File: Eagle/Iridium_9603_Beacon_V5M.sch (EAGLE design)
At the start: 99 parts, among them CON4 uFL, J1 SS4-10-3.50-X-D, Q1 DMG3415U-7, Q2 DMG3415U-7, Q3 DMG3415U-7, Q4 DMG3415U-7, Q5 2N2222, U1 MCP111T-240E/TT, U2 SPX3819-3.3, U3 LTC3225EDDB#TRMPBF, U4 MPL3115A2LGA8, U5 ATSAMD21G18_QFN, U6 MAX-M8, U7 LT1634-1,25BMCMS8, X1 32.768

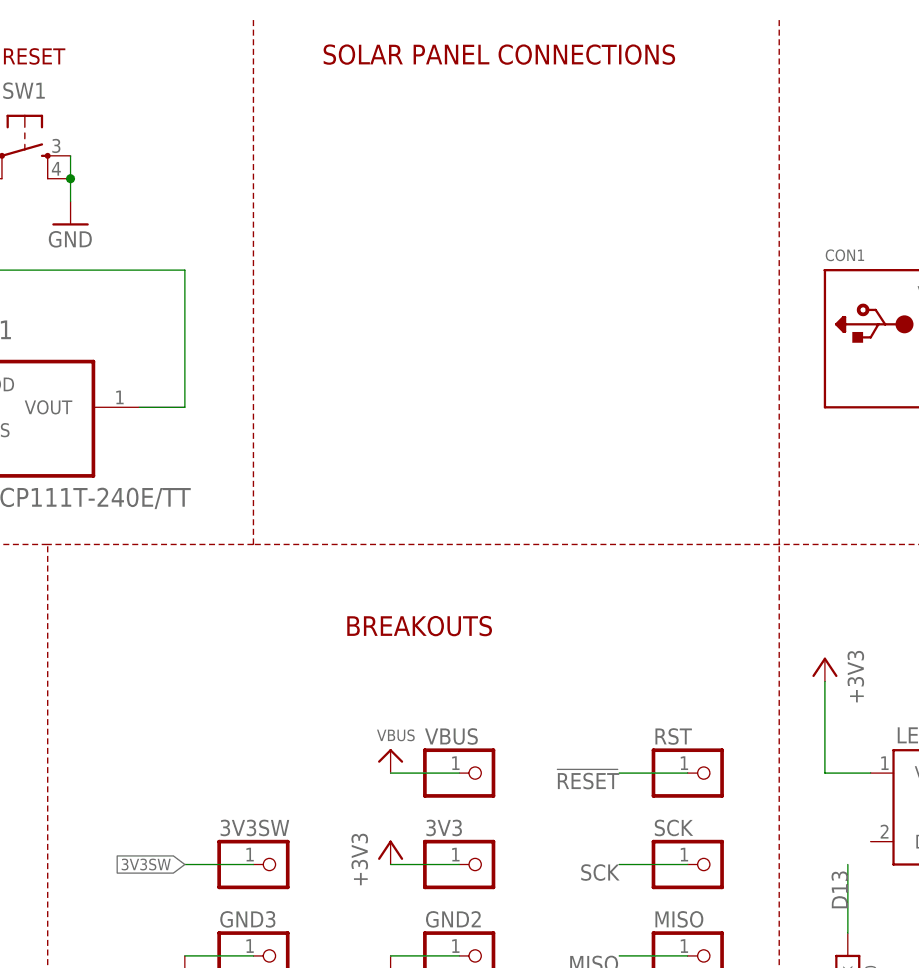
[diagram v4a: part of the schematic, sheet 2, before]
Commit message: several changes to the board layout. Switched digital I/O lines for coil reset and charger shutdown.  Added extra serial port.
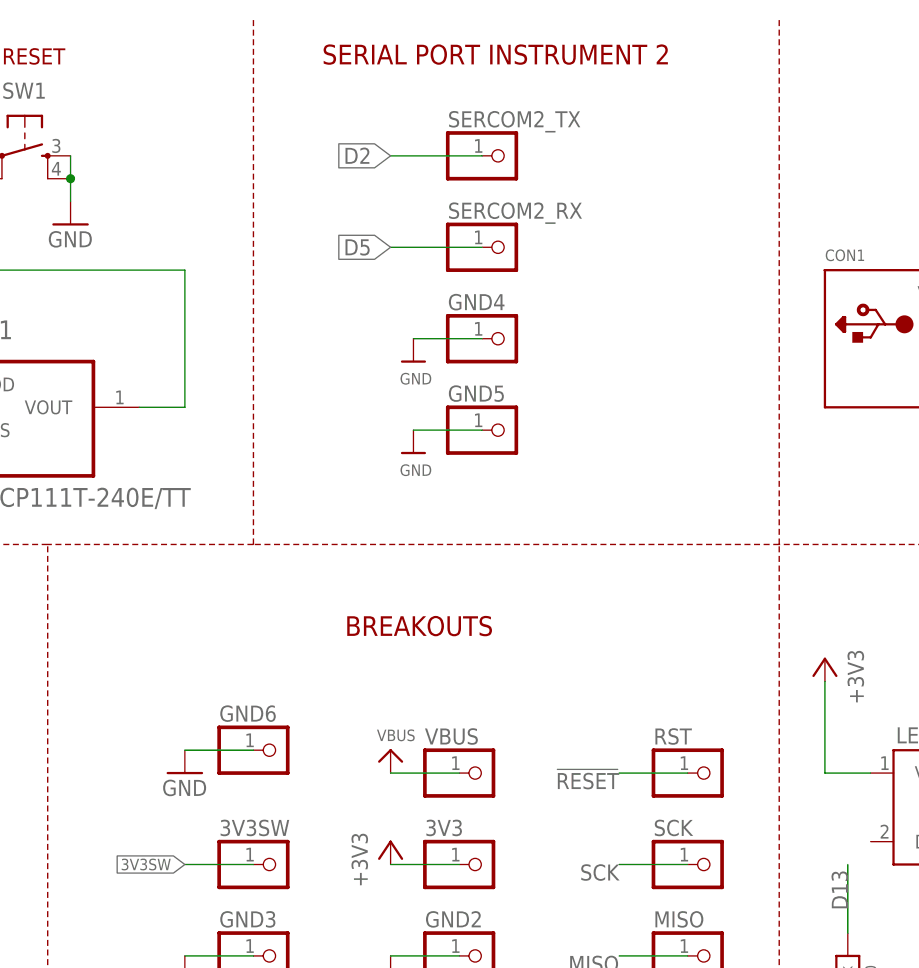
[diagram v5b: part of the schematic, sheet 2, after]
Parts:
- added GND4, GND5, GND6, SERCOM2_RX, SERCOM2_TX: (no value), adafruit:PINHD-1X1
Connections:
- net D2: now also SERCOM2_TX.1; no longer Q3.G, R13.1
- net D3: now also Q3.G, R13.1
- net D5: now also SERCOM2_RX.1; no longer R16.1, U3.~SHDN
- net D8: now also R16.1, U3.~SHDN
- net GND: now also GND4.1, GND5.1, GND6.1
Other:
- note added: "SERIAL PORT INSTRUMENT 2"
- note added: "V5M: Double AA battery capacity Added mounting holes (M3) Added SPDT Switch for power Removed Solar Power connections Moved Reset Switch to Bottom Moved D2 to D3 [Coil RESET] Moved D5 to D8 [LTC3225shutdown] Added Serial TX and RX, SERCOM2 on Pins 23 and 24"
- note removed: "SOLAR PANEL CONNECTIONS"
- note removed: "V5M: Double AA battery capacity Added mounting holes (M3) Added SPDT Switch for power Removed Solar Power connections Moved Reset Switch to Bottom"
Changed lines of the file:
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@@
 <part name="U$53" library="argol-eagle-library" deviceset="7101K2AV2QE" device=""/>
 <part name="FD3" library="SparkFun-Aesthetics" deviceset="FIDUCIAL" device="1X2"/>
+<part name="SERCOM2_TX" library="adafruit" library_urn="urn:adsk.eagle:library:420" deviceset="PINHD-1X1" device="" package3d_urn="urn:adsk.eagle:package:6240654/1"/>
+<part name="GND4" library="adafruit" library_urn="urn:adsk.eagle:library:420" deviceset="PINHD-1X1" device="" package3d_urn="urn:adsk.eagle:package:6240654/1"/>
+<part name="GND5" library="adafruit" library_urn="urn:adsk.eagle:library:420" deviceset="PINHD-1X1" device="" package3d_urn="urn:adsk.eagle:package:6240654/1"/>
+<part name="SERCOM2_RX" library="adafruit" library_urn="urn:adsk.eagle:library:420" deviceset="PINHD-1X1" device="" package3d_urn="urn:adsk.eagle:package:6240654/1"/>
+<part name="U$34" library="microbuilder" deviceset="GND" device=""/>
+<part name="U$54" library="microbuilder" deviceset="GND" device=""/>
+<part name="GND6" library="adafruit" library_urn="urn:adsk.eagle:library:420" deviceset="PINHD-1X1" device="" package3d_urn="urn:adsk.eagle:package:6240654/1"/>
+<part name="GND14" library="supply1" library_urn="urn:adsk.eagle:library:371" deviceset="GND" device=""/>
 </parts>
 <sheets>
@@
 <wire x1="134.62" y1="38.1" x2="134.62" y2="116.84" width="0.1524" layer="94" style="shortdash"/>
 <text x="238.76" y="76.2" size="2.1844" layer="94" align="bottom-center">WS2812B</text>
-<text x="165.1" y="170.18" size="2.1844" layer="94">SOLAR PANEL CONNECTIONS</text>
+<text x="165.1" y="170.18" size="2.1844" layer="94">SERIAL PORT INSTRUMENT 2</text>
 </plain>
 <instances>
@@
 <attribute name="VALUE" x="201.93" y="86.36" size="1.778" layer="96"/>
 </instance>
+<instance part="SERCOM2_TX" gate="G$1" x="185.42" y="160.02" smashed="yes">
+<attribute name="NAME" x="179.07" y="163.195" size="1.778" layer="95"/>
+<attribute name="VALUE" x="179.07" y="154.94" size="1.778" layer="96"/>
+</instance>
+<instance part="GND4" gate="G$1" x="185.42" y="139.7" smashed="yes">
+<attribute name="NAME" x="179.07" y="142.875" size="1.778" layer="95"/>
+<attribute name="VALUE" x="179.07" y="134.62" size="1.778" layer="96"/>
+</instance>
+<instance part="GND5" gate="G$1" x="185.42" y="129.54" smashed="yes">
+<attribute name="NAME" x="179.07" y="132.715" size="1.778" layer="95"/>
+<attribute name="VALUE" x="179.07" y="124.46" size="1.778" layer="96"/>
+</instance>
+<instance part="SERCOM2_RX" gate="G$1" x="185.42" y="149.86" smashed="yes">
+<attribute name="NAME" x="179.07" y="153.035" size="1.778" layer="95"/>
+<attribute name="VALUE" x="179.07" y="144.78" size="1.778" layer="96"/>
+</instance>
+<instance part="U$34" gate="G$1" x="175.26" y="127" smashed="yes">
+<attribute name="VALUE" x="173.736" y="124.46" size="1.27" layer="96"/>
+</instance>
+<instance part="U$54" gate="G$1" x="175.26" y="137.16" smashed="yes">
+<attribute name="VALUE" x="173.736" y="134.62" size="1.27" layer="96"/>
+</instance>
+<instance part="GND6" gate="G$1" x="160.02" y="93.98" smashed="yes">
+<attribute name="NAME" x="153.67" y="97.155" size="1.778" layer="95"/>
+<attribute name="VALUE" x="153.67" y="88.9" size="1.778" layer="96"/>
+</instance>
+<instance part="GND14" gate="1" x="149.86" y="91.44" smashed="yes">
+<attribute name="VALUE" x="147.32" y="88.9" size="1.778" layer="96"/>
+</instance>
 </instances>
 <busses>
@@
 <pinref part="GND9" gate="1" pin="GND"/>
 <wire x1="223.52" y1="53.34" x2="223.52" y2="48.26" width="0.1524" layer="91"/>
+</segment>
+<segment>
+<pinref part="U$54" gate="G$1" pin="GND"/>
+<pinref part="GND4" gate="G$1" pin="1"/>
+<wire x1="175.26" y1="139.7" x2="182.88" y2="139.7" width="0.1524" layer="91"/>
+</segment>
+<segment>
+<pinref part="U$34" gate="G$1" pin="GND"/>
+<pinref part="GND5" gate="G$1" pin="1"/>
+<wire x1="175.26" y1="129.54" x2="182.88" y2="129.54" width="0.1524" layer="91"/>
+</segment>
+<segment>
+<pinref part="GND14" gate="1" pin="GND"/>
+<pinref part="GND6" gate="G$1" pin="1"/>
+<wire x1="149.86" y1="93.98" x2="157.48" y2="93.98" width="0.1524" layer="91"/>
 </segment>
 </net>
@@
 <label x="109.22" y="50.8" size="1.778" layer="95"/>
 </segment>
+<segment>
+<pinref part="SERCOM2_RX" gate="G$1" pin="1"/>
+<wire x1="182.88" y1="149.86" x2="172.72" y2="149.86" width="0.1524" layer="91"/>
+<label x="172.72" y="149.86" size="1.778" layer="95" rot="R180" xref="yes"/>
+</segment>
 </net>
 <net name="D1" class="0">
@@
 <wire x1="101.6" y1="53.34" x2="119.38" y2="53.34" width="0.1524" layer="91"/>
 <label x="109.22" y="53.34" size="1.778" layer="95"/>
+</segment>
+<segment>
+<pinref part="SERCOM2_TX" gate="G$1" pin="1"/>
+<wire x1="182.88" y1="160.02" x2="172.72" y2="160.02" width="0.1524" layer="91"/>
+<label x="172.72" y="160.02" size="1.778" layer="95" rot="R180" xref="yes"/>
 </segment>
 </net>
@@
 </busses>
 <nets>
-<net name="D5" class="0">
-<segment>
-<label x="68.58" y="111.76" size="1.27" layer="95" rot="R180" xref="yes"/>
-<pinref part="U3" gate="G$1" pin="~SHDN"/>
-<wire x1="68.58" y1="111.76" x2="71.12" y2="111.76" width="0.1524" layer="91"/>
-<pinref part="R16" gate="G$1" pin="1"/>
-<wire x1="71.12" y1="111.76" x2="83.82" y2="111.76" width="0.1524" layer="91"/>
-<wire x1="71.12" y1="101.6" x2="71.12" y2="111.76" width="0.1524" layer="91"/>
-<junction x="71.12" y="111.76"/>
-</segment>
-</net>
 <net name="N$9" class="0">
 <segment>
@@
 </segment>
 </net>
+<net name="D8" class="0">
+<segment>
+<label x="68.58" y="111.76" size="1.27" layer="95" rot="R180" xref="yes"/>
+<pinref part="U3" gate="G$1" pin="~SHDN"/>
+<wire x1="68.58" y1="111.76" x2="71.12" y2="111.76" width="0.1524" layer="91"/>
+<pinref part="R16" gate="G$1" pin="1"/>
+<wire x1="71.12" y1="111.76" x2="83.82" y2="111.76" width="0.1524" layer="91"/>
+<wire x1="71.12" y1="101.6" x2="71.12" y2="111.76" width="0.1524" layer="91"/>
+<junction x="71.12" y="111.76"/>
+</segment>
+</net>
 </nets>
 </sheet>
@@
 </segment>
 </net>
-<net name="D2" class="0">
-<segment>
-<pinref part="Q3" gate="G$1" pin="G"/>
-<pinref part="R13" gate="G$1" pin="1"/>
-<wire x1="71.12" y1="101.6" x2="63.5" y2="101.6" width="0.1524" layer="91"/>
-<wire x1="63.5" y1="101.6" x2="48.26" y2="101.6" width="0.1524" layer="91"/>
-<junction x="63.5" y="101.6"/>
-<label x="48.26" y="101.6" size="1.778" layer="95" rot="R180" xref="yes"/>
-</segment>
-</net>
 <net name="RESET_RELAY" class="0">
 <segment>
@@
 <junction x="101.6" y="134.62"/>
 <label x="88.9" y="134.62" size="1.778" layer="95" rot="R180" xref="yes"/>
+</segment>
+</net>
+<net name="D3" class="0">
+<segment>
+<pinref part="Q3" gate="G$1" pin="G"/>
+<pinref part="R13" gate="G$1" pin="1"/>
+<wire x1="71.12" y1="101.6" x2="63.5" y2="101.6" width="0.1524" layer="91"/>
+<wire x1="63.5" y1="101.6" x2="50.8" y2="101.6" width="0.1524" layer="91"/>
+<junction x="63.5" y="101.6"/>
+<label x="50.8" y="101.6" size="1.778" layer="95" rot="R180" xref="yes"/>
 </segment>
 </net>
@@
 Added a pad for an external reset switch
 Added a pad for a battery power switch</text>
-<text x="157.48" y="149.86" size="2.54" layer="91" align="top-left">V5M:
+<text x="170.18" y="149.86" size="2.54" layer="91" align="top-left">V5M:
 Double AA battery capacity
 Added mounting holes (M3)
 Added SPDT Switch for power
 Removed Solar Power connections
-Moved Reset Switch to Bottom</text>
+Moved Reset Switch to Bottom
+Moved D2 to D3 [Coil RESET]
+Moved D5 to D8 [LTC3225shutdown]
+Added Serial TX and RX, SERCOM2 on Pins 23 and 24</text>
 </plain>
 <instances>

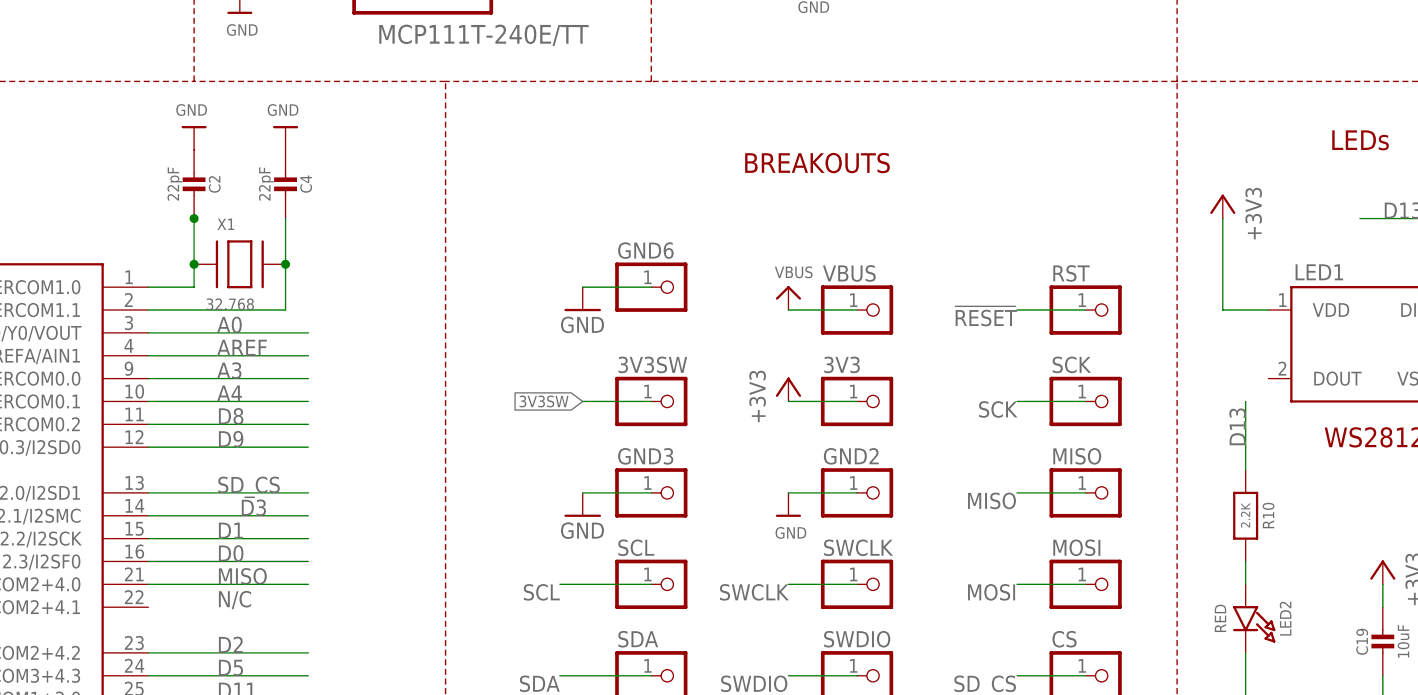
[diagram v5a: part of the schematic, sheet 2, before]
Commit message: updated CAD file, BOM, Gerber files generated for initial version of the board
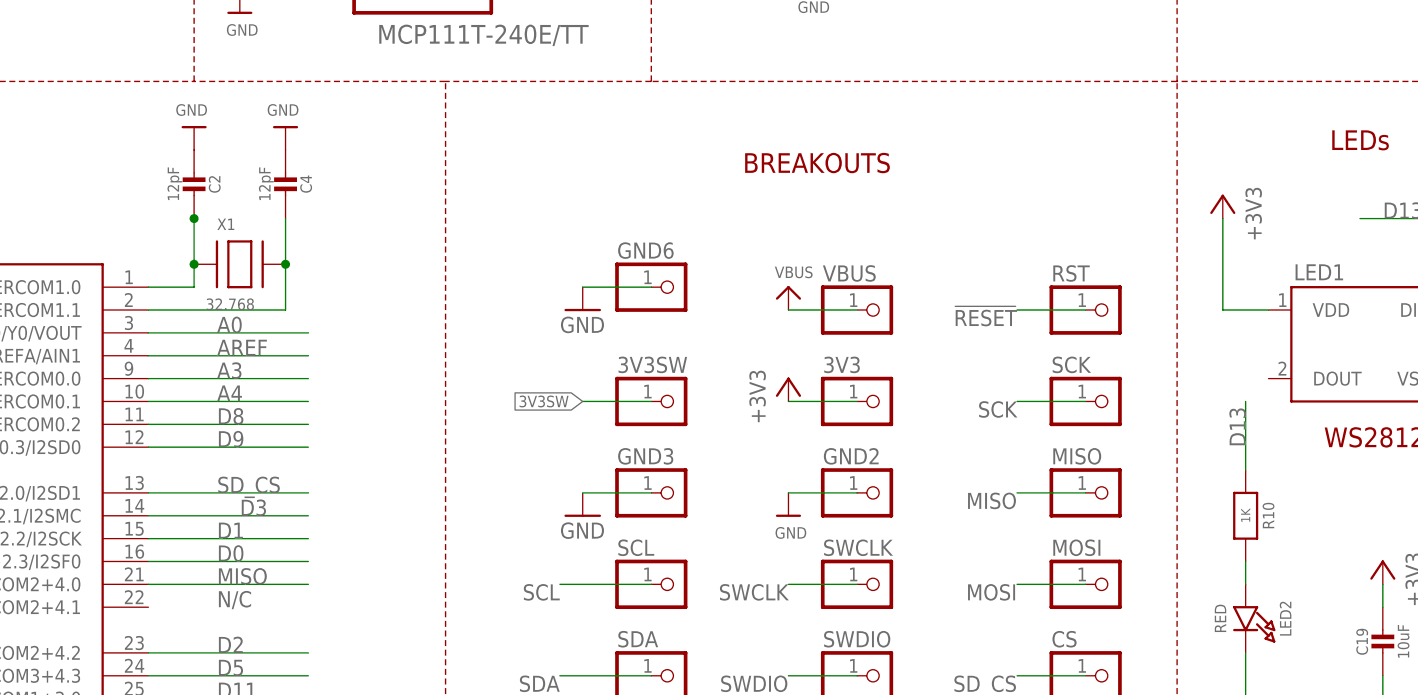
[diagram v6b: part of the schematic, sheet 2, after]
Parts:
- C2, C4: value 22pF -> 12pF
- R10: value 2.2K -> 1K
- renumbered U$53 to U53
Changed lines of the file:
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@@
 <part name="C1" library="microbuilder" deviceset="CAP_CERAMIC" device="0603_NO" value="1uF"/>
 <part name="U$6" library="microbuilder" deviceset="GND" device=""/>
-<part name="C2" library="microbuilder" deviceset="CAP_CERAMIC" device="0603_NO" value="22pF"/>
-<part name="C4" library="microbuilder" deviceset="CAP_CERAMIC" device="0603_NO" value="22pF"/>
+<part name="C2" library="microbuilder" deviceset="CAP_CERAMIC" device="0603_NO" value="12pF"/>
+<part name="C4" library="microbuilder" deviceset="CAP_CERAMIC" device="0603_NO" value="12pF"/>
 <part name="U$8" library="microbuilder" deviceset="GND" device=""/>
 <part name="U$10" library="microbuilder" deviceset="GND" device=""/>
@@
 <part name="U$44" library="microbuilder" deviceset="GND" device=""/>
 <part name="LED2" library="microbuilder" deviceset="LED" device="0805_NOOUTLINE" value="RED"/>
-<part name="R10" library="microbuilder" deviceset="RESISTOR" device="_0603_NOOUT" value="2.2K"/>
+<part name="R10" library="microbuilder" deviceset="RESISTOR" device="_0603_NOOUT" value="1K"/>
 <part name="GND9" library="supply1" deviceset="GND" device=""/>
 <part name="U$45" library="microbuilder" deviceset="VBUS" device=""/>
@@
 <part name="BAT5" library="SparkFun-Electromechanical" deviceset="BATTERY" device="KEYSTONE92"/>
 <part name="BAT6" library="SparkFun-Electromechanical" deviceset="BATTERY" device="KEYSTONE92"/>
-<part name="U$53" library="argol-eagle-library" deviceset="7101K2AV2QE" device=""/>
+<part name="U53" library="argol-eagle-library" deviceset="7101K2AV2QE" device=""/>
 <part name="FD3" library="SparkFun-Aesthetics" deviceset="FIDUCIAL" device="1X2"/>
 <part name="SERCOM2_TX" library="adafruit" library_urn="urn:adsk.eagle:library:420" deviceset="PINHD-1X1" device="" package3d_urn="urn:adsk.eagle:package:6240654/1"/>
@@
 <attribute name="VALUE" x="229.87" y="85.09" size="1.778" layer="96" rot="R270"/>
 </instance>
-<instance part="U$53" gate="G$1" x="193.04" y="71.12" smashed="yes" rot="R180"/>
+<instance part="U53" gate="G$1" x="193.04" y="71.12" smashed="yes" rot="R180"/>
 <instance part="FD3" gate="G$1" x="231.14" y="35.56" smashed="yes"/>
 </instances>
@@
 <pinref part="GND" gate="G$1" pin="1"/>
 <wire x1="210.312" y1="61.722" x2="218.44" y2="61.722" width="0.1524" layer="91"/>
-<pinref part="U$53" gate="G$1" pin="P$1"/>
+<pinref part="U53" gate="G$1" pin="P$1"/>
 <wire x1="180.34" y1="66.04" x2="180.34" y2="61.722" width="0.1524" layer="91"/>
 <wire x1="180.34" y1="61.722" x2="210.312" y2="61.722" width="0.1524" layer="91"/>
@@
 <junction x="218.44" y="76.2"/>
 <junction x="210.312" y="71.882"/>
-<pinref part="U$53" gate="G$1" pin="P$2"/>
+<pinref part="U53" gate="G$1" pin="P$2"/>
 <wire x1="210.312" y1="71.882" x2="210.312" y2="71.12" width="0.1524" layer="91"/>
 <wire x1="210.312" y1="71.12" x2="198.12" y2="71.12" width="0.1524" layer="91"/>
